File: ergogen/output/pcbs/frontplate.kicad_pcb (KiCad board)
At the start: 2 copper layers, 129.8 x 107.9 mm, 5 parts

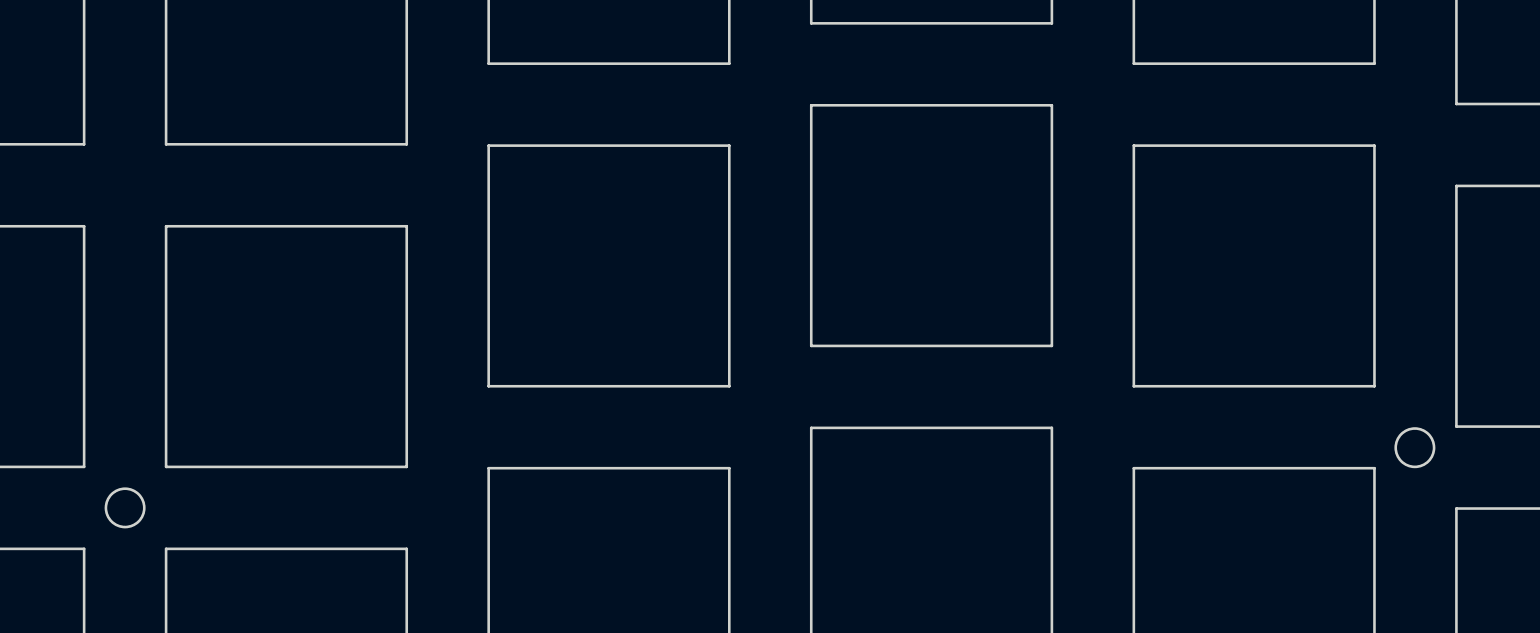
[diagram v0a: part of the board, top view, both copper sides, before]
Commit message: feat: reversible pg1316s switch footprint
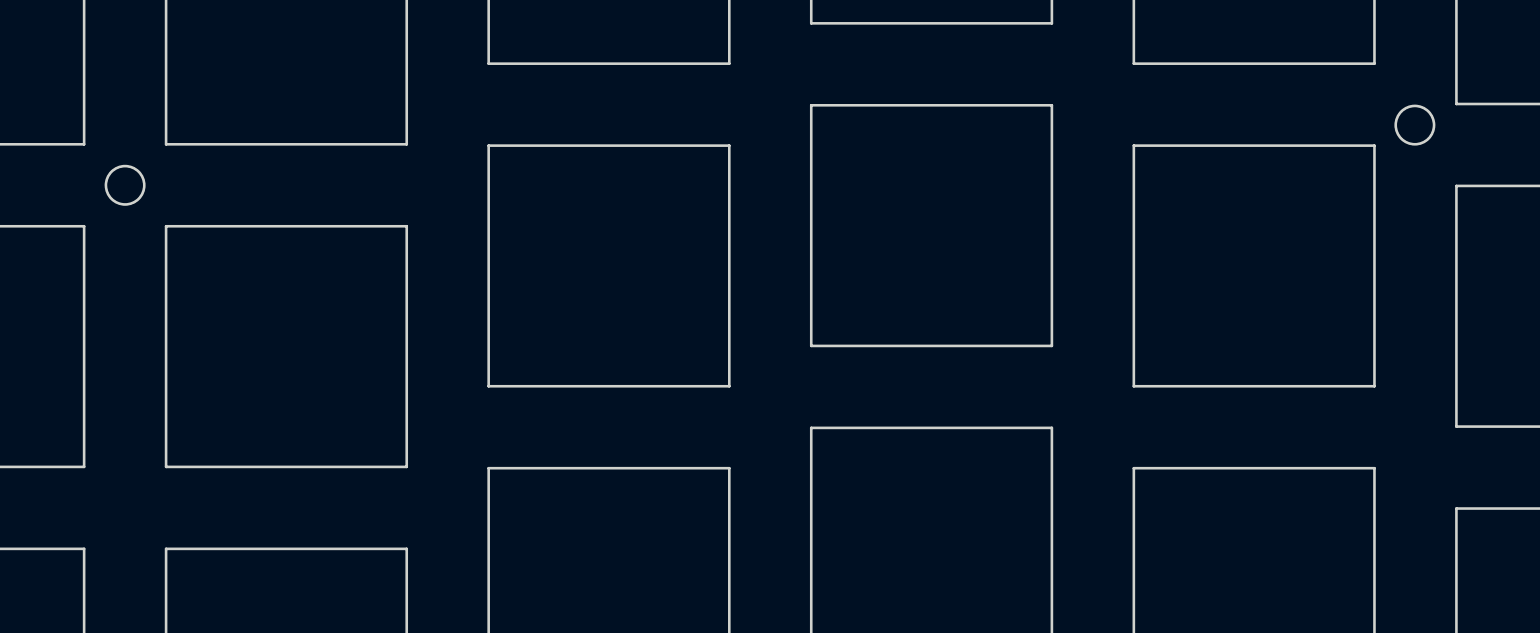
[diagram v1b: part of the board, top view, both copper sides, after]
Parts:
- moved MH1 18.5 mm to (109.2, 53.8)
- moved MH3 18.5 mm to (183.2, 50.3)
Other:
- outline, holes or cut-outs redrawn
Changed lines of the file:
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@@
   (title_block
     (title "frontplate")
-    (date "2025-03-01")
+    (date "2025-03-02")
     (rev "0.2")
     (company "ceoloide")
@@
   (footprint "ceoloide:mounting_hole_npth"
     (layer "F.Cu")
-    (at 109.25 72.25 0)
+    (at 109.25 53.75 0)
     (property "Reference" "MH1"
       (at 0 2.55 0)
@@
   (footprint "ceoloide:mounting_hole_npth"
     (layer "F.Cu")
-    (at 183.218 68.7985 0)
+    (at 183.218 50.298500000000004 0)
     (property "Reference" "MH3"
       (at 0 2.55 0)
@@
 (gr_line (start 204.48826759999997 111.5216728) (end 197.5882676 123.4728234) (layer Edge.Cuts) (stroke (width 0.15) (type default)))
 (gr_line (start 197.5882676 123.4728234) (end 209.53941819999997 130.37282340000002) (layer Edge.Cuts) (stroke (width 0.15) (type default)))
-(gr_circle (center 109.25 72.25) (end 110.35 72.25) (layer Edge.Cuts) (stroke (width 0.15) (type default)) (fill none))
+(gr_circle (center 109.25 53.75) (end 110.35 53.75) (layer Edge.Cuts) (stroke (width 0.15) (type default)) (fill none))
 (gr_circle (center 109.25 90.75) (end 110.35 90.75) (layer Edge.Cuts) (stroke (width 0.15) (type default)) (fill none))
-(gr_circle (center 183.218 68.7985) (end 184.31799999999998 68.7985) (layer Edge.Cuts) (stroke (width 0.15) (type default)) (fill none))
+(gr_circle (center 183.218 50.298500000000004) (end 184.31799999999998 50.298500000000004) (layer Edge.Cuts) (stroke (width 0.15) (type default)) (fill none))
 (gr_circle (center 151.157 107.615) (end 152.257 107.615) (layer Edge.Cuts) (stroke (width 0.15) (type default)) (fill none))
 (gr_circle (center 196.7245951 115.0067481) (end 197.82459509999998 115.0067481) (layer Edge.Cuts) (stroke (width 0.15) (type default)) (fill none))
